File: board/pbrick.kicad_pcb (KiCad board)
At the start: 4 copper layers, 24 x 44 mm, 59 parts, among them J1 UJC-HP-3-SMT-TR, J2 TC2030-IDC-NL, J3 U.FL2PIN, J4 QWIIC, M0 5055680471, M1 5055680471, Q1 SSM6J507NU, Q2 SSM6J507NU, U1 MIC5219-3.3YML-TR, U2 ADP3330ARTZ-5-RL7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

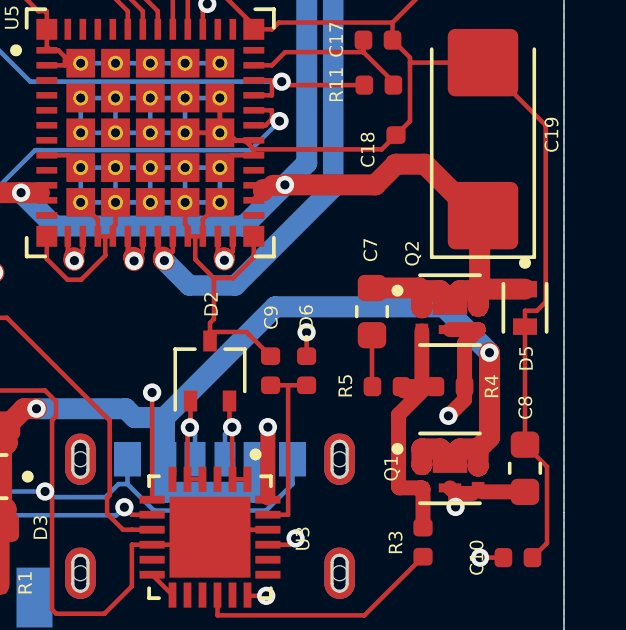
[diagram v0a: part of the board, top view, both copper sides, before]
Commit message: Correct schematic defect where Q2 was not routed on both ends
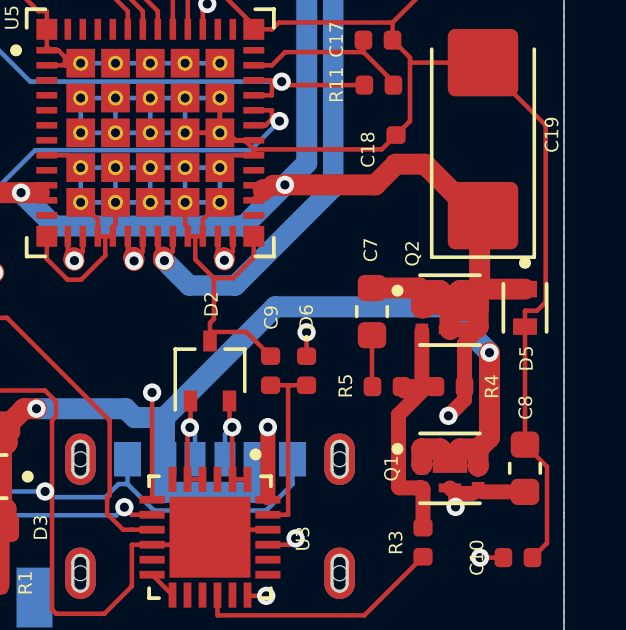
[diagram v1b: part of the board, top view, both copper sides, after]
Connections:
- C8 pad 2: Net-(C8-Pad2) -> VDD
- J1 pad S1: (no net) -> Net-(J1-PadS1)
- J1 pad S2: (no net) -> Net-(J1-PadS1)
- J1 pad S3: (no net) -> Net-(J1-PadS1)
- J1 pad S4: (no net) -> Net-(J1-PadS1)
- J2 pad 6: (no net) -> Net-(J2-Pad6)
- M0 pad S1: (no net) -> Net-(M0-PadS1)
- M0 pad S2: (no net) -> Net-(M0-PadS1)
- M1 pad S1: (no net) -> Net-(M1-PadS1)
- M1 pad S2: (no net) -> Net-(M1-PadS1)
- PROTEUS-III1 pad 13: (no net) -> /P1.08
- PROTEUS-III1 pad 14: (no net) -> /P1.09
- PROTEUS-III1 pad 15: (no net) -> /P0.11
- PROTEUS-III1 pad 16: (no net) -> /P0.12
- PROTEUS-III1 pad 17: (no net) -> /P0.03
- PROTEUS-III1 pad 7: (no net) -> /P0.02
- PROTEUS-III1 pad B4: (no net) -> /P1.00
- PROTEUS-III1 pad B5: (no net) -> /P0.21
- PROTEUS-III1 pad B6: (no net) -> /P0.07
- Q1 pad 4: Net-(C8-Pad2) -> VDD
- Q1 pad 8: Net-(C8-Pad2) -> VDD
- Q2 pad 4: Net-(C8-Pad2) -> VDD
- Q2 pad 8: Net-(C8-Pad2) -> VDD
- R4 pad 1: Net-(C8-Pad2) -> VDD
- U1 pad 5: (no net) -> Net-(U1-Pad5)
- U2 pad 3: (no net) -> Net-(U2-Pad3)
- U2 pad 5: (no net) -> Net-(U2-Pad5)
- U3 pad 11: (no net) -> Net-(U3-Pad11)
- U3 pad 14: (no net) -> Net-(U3-Pad14)
- U3 pad 15: (no net) -> Net-(U3-Pad15)
- U3 pad 17: (no net) -> Net-(U3-Pad17)
- U3 pad 19: (no net) -> Net-(U3-Pad19)
- U3 pad 20: (no net) -> Net-(U3-Pad20)
- U3 pad 24: Net-(C8-Pad2) -> VDD
- U3 pad 6: (no net) -> Net-(U3-Pad6)
- U5 pad 47: (no net) -> Net-(U5-Pad47)
- U5 pad 48: (no net) -> Net-(U5-Pad48)
- U6 pad 5: (no net) -> Net-(U6-Pad5)
- U7 pad 14: (no net) -> /PCA9624_7
- U7 pad 5: (no net) -> /PCA9624_0
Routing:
- net VDD: track 84.0 -> 106.9 mm, vias 3 -> 6
- net Net-(C8-Pad2): track 19.2 -> 0.00 mm, vias 3 -> 0

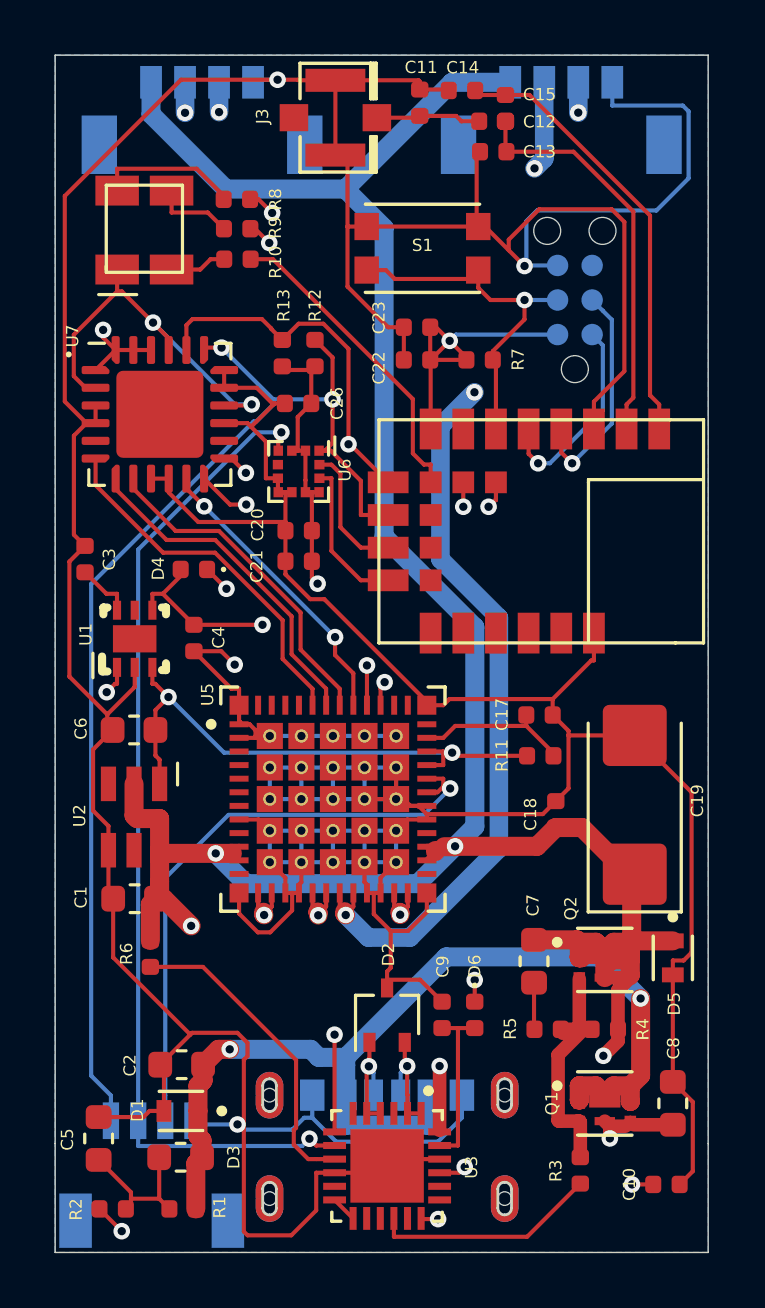
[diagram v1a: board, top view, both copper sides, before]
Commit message: 5v regulator has operational capacity from 2.7-20v (tested)   - removing extra diode and 2.7v line as 5v => 3.3v works at 5v input
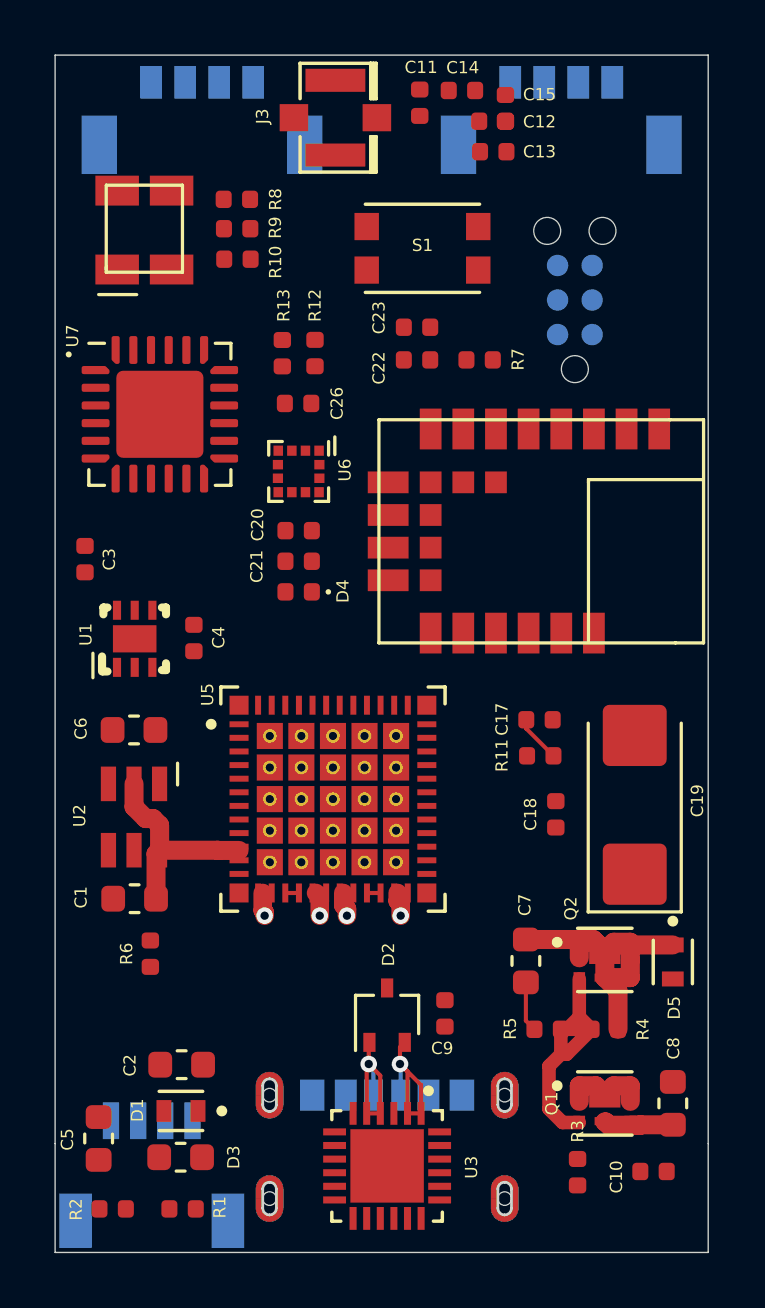
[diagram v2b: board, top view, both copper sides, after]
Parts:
- removed D6: D_Schottky, Diode_SMD:D_0402_1005Metric
- moved D4 3.94 mm to (128.9, 109.7)
- moved C10 0.67 mm to (142.0, 131.0)
- moved C7 0.30 mm to (137.3, 123.3)
- moved C17 0.17 mm to (137.8, 114.4)
- moved D5 0.15 mm to (142.7, 123.3)
- moved R3 0.12 mm to (139.2, 131.1)
- moved C9 0.12 mm to (134.3, 125.2)
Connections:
- net +2V8 renamed Net-(C9-Pad2)
- C22 pad 1: +3.3VA -> 3.3V
- C23 pad 1: +3.3VA -> 3.3V
- C4 pad 1: 3.3V -> Net-(C4-Pad1)
- D4 pad 1: +3.3VA -> 3.3V
- D4 pad 2: 3.3V -> Net-(C4-Pad1)
- J1 pad S1: Net-(J1-PadS1) -> (no net)
- J1 pad S2: Net-(J1-PadS1) -> (no net)
- J1 pad S3: Net-(J1-PadS1) -> (no net)
- J1 pad S4: Net-(J1-PadS1) -> (no net)
- J2 pad 1: +3.3VA -> 3.3V
- J2 pad 6: Net-(J2-Pad6) -> (no net)
- M0 pad S1: Net-(M0-PadS1) -> (no net)
- M0 pad S2: Net-(M0-PadS1) -> (no net)
- M1 pad S1: Net-(M1-PadS1) -> (no net)
- M1 pad S2: Net-(M1-PadS1) -> (no net)
- PROTEUS-III1 pad 13: /P1.08 -> (no net)
- PROTEUS-III1 pad 14: /P1.09 -> (no net)
- PROTEUS-III1 pad 15: /P0.11 -> (no net)
- PROTEUS-III1 pad 16: /P0.12 -> (no net)
- PROTEUS-III1 pad 17: /P0.03 -> (no net)
- PROTEUS-III1 pad 7: /P0.02 -> (no net)
- PROTEUS-III1 pad 8: +3.3VA -> 3.3V
- PROTEUS-III1 pad B4: /P1.00 -> (no net)
- PROTEUS-III1 pad B5: /P0.21 -> (no net)
- PROTEUS-III1 pad B6: /P0.07 -> (no net)
- R7 pad 1: +3.3VA -> 3.3V
- U1 pad 4: 3.3V -> Net-(C4-Pad1)
- U1 pad 5: Net-(U1-Pad5) -> (no net)
- U2 pad 3: Net-(U2-Pad3) -> (no net)
- U2 pad 5: Net-(U2-Pad5) -> (no net)
- U3 pad 11: Net-(U3-Pad11) -> (no net)
- U3 pad 14: Net-(U3-Pad14) -> (no net)
- U3 pad 15: Net-(U3-Pad15) -> (no net)
- U3 pad 17: Net-(U3-Pad17) -> (no net)
- U3 pad 19: Net-(U3-Pad19) -> (no net)
- U3 pad 20: Net-(U3-Pad20) -> (no net)
- U3 pad 6: Net-(U3-Pad6) -> (no net)
- U5 pad 47: Net-(U5-Pad47) -> (no net)
- U5 pad 48: Net-(U5-Pad48) -> (no net)
- U6 pad 5: Net-(U6-Pad5) -> (no net)
- U7 pad 14: /PCA9624_7 -> (no net)
- U7 pad 25: (no net) -> GND
- U7 pad 5: /PCA9624_0 -> (no net)
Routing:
- net GND: track 356.7 -> 1.00 mm, vias 5 -> 0
- net VDD: track 106.9 -> 24.4 mm, vias 6 -> 0
- net /P0.22: track 75.6 -> 0.00 mm, vias 3 -> 0
- net +3.3VA: track 56.9 -> 0.00 mm, vias 3 -> 0
- net /P0.19: track 53.5 -> 0.00 mm, vias 3 -> 0
- net 5V: track 52.9 -> 0.00 mm, vias 5 -> 0
- net 3.3V: track 50.9 -> 0.00 mm, vias 3 -> 0
- net /M1_0: track 41.5 -> 0.89 mm, vias 2 -> 1
- net /M0_0: track 40.7 -> 0.89 mm, vias 3 -> 1
- net VBUS: track 37.6 -> 3.29 mm, vias 2 -> 0
- net /M0_1: track 34.9 -> 0.88 mm, vias 2 -> 1
- net /M1_1: track 33.7 -> 0.86 mm, vias 2 -> 1
- net /ANT: track 16.3 -> 0.00 mm
- net /P0.09: track 16.1 -> 0.00 mm, vias 2 -> 0
- net /RF: track 14.8 -> 0.00 mm
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- removed copper zone on B.Cu, net GND
- removed copper zone on GND, net GND
- removed copper zone on M.Cu, net GND
- removed copper zone on M.Cu, net VBUS
- removed copper zone on M.Cu, net VDD

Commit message: Updating PCB routing
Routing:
- net GND: track 1.00 -> 303.0 mm, vias 0 -> 3
- net VDD: track 24.4 -> 112.5 mm, vias 0 -> 4
- net 3.3V: track 0.00 -> 63.0 mm, vias 0 -> 3
- net /P0.19: track 0.00 -> 55.3 mm, vias 0 -> 3
- net /P0.22: track 0.00 -> 51.8 mm, vias 0 -> 3
- net 5V: track 0.00 -> 49.8 mm, vias 0 -> 5
- net /M1_0: track 0.89 -> 36.3 mm, vias 1 -> 2
- net /M0_0: track 0.89 -> 36.1 mm, vias 1 -> 2
- net /M1_1: track 0.86 -> 35.4 mm, vias 1 -> 2
- net /M0_1: track 0.88 -> 34.2 mm
- net VBUS: track 3.29 -> 32.9 mm, vias 0 -> 2
- net /P0.09: track 0.00 -> 16.3 mm, vias 0 -> 2
- net /ANT: track 0.00 -> 15.9 mm
- net /RF: track 0.00 -> 14.4 mm
- net Net-(R2-Pad2): track 0.00 -> 13.8 mm, vias 0 -> 2
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- added copper zone on B.Cu, net GND
- added copper zone on GND, net GND
- added copper zone on M.Cu, net GND
- added copper zone on M.Cu, net VBUS
- added copper zone on M.Cu, net VDD

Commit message: Updating PCB layout
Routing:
- net VDD: track 112.5 -> 106.7 mm, vias 4 -> 5
- net VBUS: track 32.9 -> 37.4 mm
- net GND: track 303.0 -> 307.0 mm

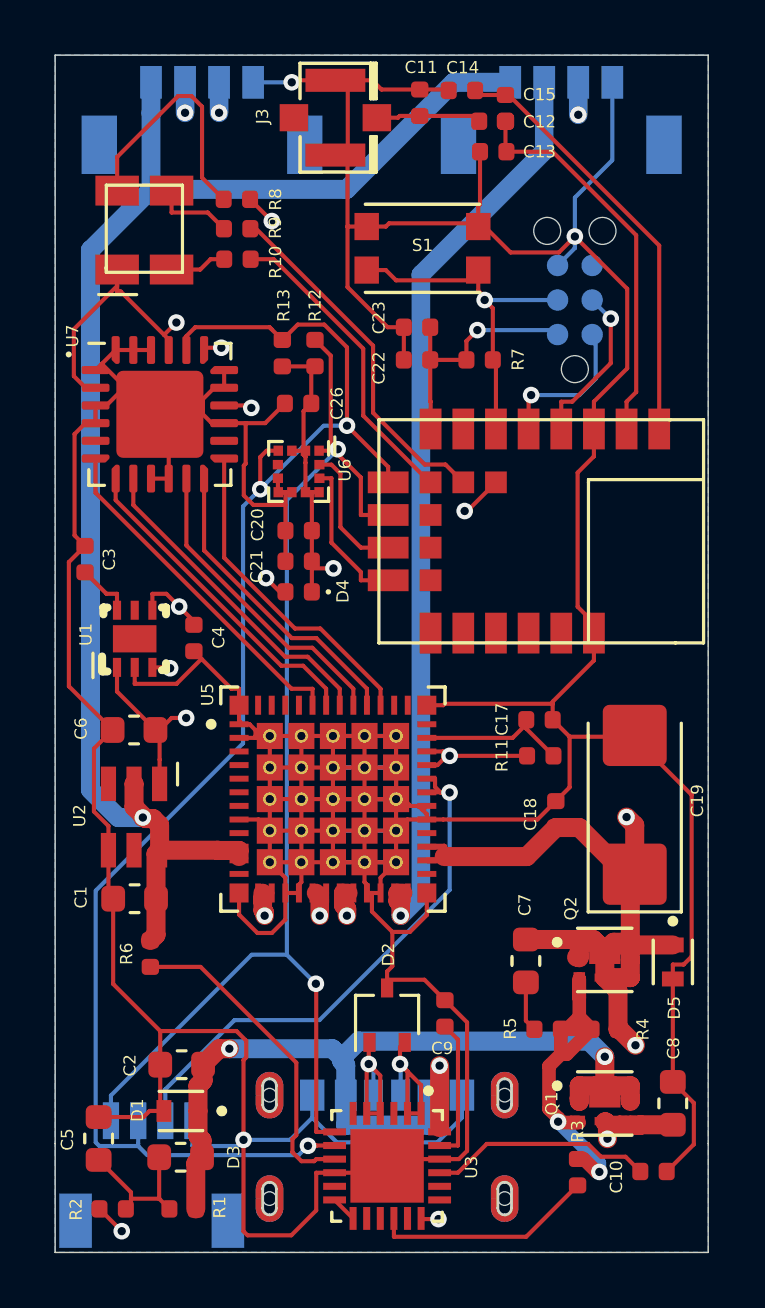
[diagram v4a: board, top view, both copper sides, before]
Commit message: Updating PCB to resolve an issue with PCA9624 OE being HIGH instead of Controller - Added PCA9624 library definition (untested) - Convert pbrick_motor to use PCA9624 driver
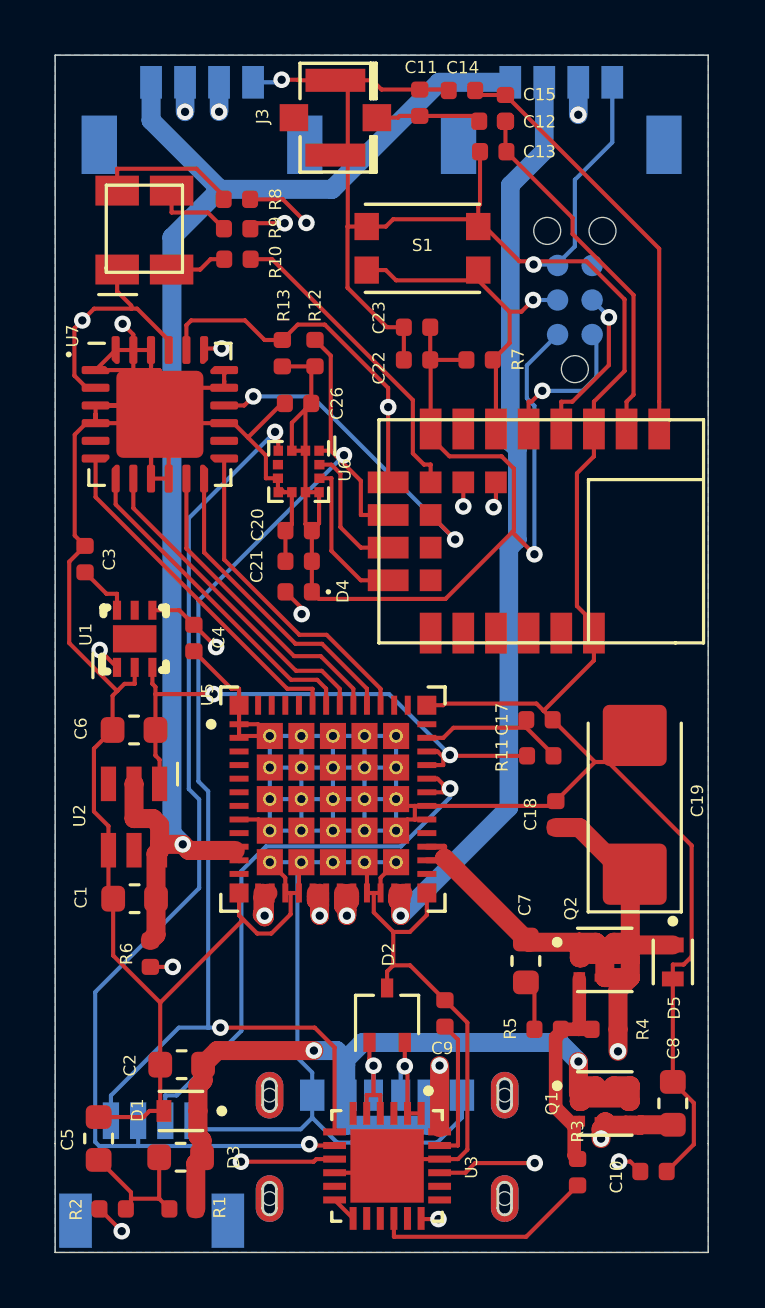
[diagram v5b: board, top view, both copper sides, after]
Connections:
- J2 pad 6: (no net) -> Net-(J2-Pad6)
- PROTEUS-III1 pad 13: (no net) -> /P1.08
- PROTEUS-III1 pad 14: (no net) -> /P1.09
- PROTEUS-III1 pad 15: (no net) -> /P0.11
- PROTEUS-III1 pad 16: (no net) -> /P0.12
- PROTEUS-III1 pad 17: (no net) -> /P0.03
- PROTEUS-III1 pad 7: (no net) -> /P0.02
- PROTEUS-III1 pad B4: (no net) -> /P1.00
- PROTEUS-III1 pad B5: (no net) -> /P0.21
- PROTEUS-III1 pad B6: (no net) -> /P0.07
- U1 pad 5: (no net) -> Net-(U1-Pad5)
- U2 pad 3: (no net) -> Net-(U2-Pad3)
- U2 pad 5: (no net) -> Net-(U2-Pad5)
- U3 pad 11: (no net) -> Net-(U3-Pad11)
- U3 pad 14: (no net) -> Net-(U3-Pad14)
- U3 pad 15: (no net) -> Net-(U3-Pad15)
- U3 pad 17: (no net) -> Net-(U3-Pad17)
- U3 pad 19: (no net) -> Net-(U3-Pad19)
- U3 pad 20: (no net) -> Net-(U3-Pad20)
- U3 pad 6: (no net) -> Net-(U3-Pad6)
- U5 pad 47: (no net) -> Net-(U5-Pad47)
- U5 pad 48: (no net) -> Net-(U5-Pad48)
- U6 pad 5: (no net) -> Net-(U6-Pad5)
- U7 pad 14: (no net) -> /PCA9624_7
- U7 pad 16: 5V -> /P1.00
- U7 pad 5: (no net) -> /PCA9624_0
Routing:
- net GND: track 307.0 -> 325.3 mm
- net 3.3V: track 63.0 -> 75.3 mm, vias 3 -> 2
- net /P1.00: track 0.00 -> 12.1 mm, vias 0 -> 2
- net Net-(Q1-Pad3): track 14.7 -> 8.53 mm, vias 2 -> 0
- net /M0_0: track 36.1 -> 40.3 mm
- net Net-(LED1-Pad3): track 9.18 -> 5.26 mm
- net VBUS: track 37.4 -> 33.5 mm
- net /P0.19: track 55.8 -> 59.7 mm
- net /M1_0: track 36.3 -> 38.7 mm
- net Net-(D2-Pad2): track 6.59 -> 4.28 mm
- net VDD: track 106.7 -> 108.9 mm, vias 5 -> 4
- net /P0.10: track 13.1 -> 15.4 mm, vias 0 -> 2
- net 5V: track 49.8 -> 47.9 mm, vias 5 -> 4
- net Net-(D2-Pad1): track 6.36 -> 4.93 mm
- net /M1_1: track 35.4 -> 34.1 mm
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- removed copper zone on M.Cu, net GND

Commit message: Updating layout
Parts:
- added 3V3: Val**, Connectors:PAD.02X.02, F.Cu at (129.4, 110.8)
- added 5V: Val**, Connectors:PAD.02X.02, F.Cu at (122.3, 99.4)
- added VBUS: Val**, Connectors:PAD.02X.02, F.Cu at (138.0, 128.1)
- added VDD: Val**, Connectors:PAD.02X.02, F.Cu at (138.4, 119.5)
- U7: footprint Package_DFN_QFN:QFN-24-1EP_5x5mm_P0.65mm_EP3.2x3.2mm -> Package_DFN_QFN:QFN-24-1EP_4x4mm_P0.5mm_EP2.65x2.65mm_ThermalVias
- moved C13 1.46 mm to (134.9, 94.5)
- moved C12 1.46 mm to (134.9, 93.3)
- moved C15 1.46 mm to (135.4, 92.8)
- moved R8 1.10 mm to (126.7, 96.4)
- moved R9 1.08 mm to (126.7, 95.3)
- moved C23 0.93 mm to (133.8, 100.8)
- moved R7 0.87 mm to (136.1, 102.0)
- moved C22 0.87 mm to (133.8, 102.0)
- moved J2 0.45 mm to (138.7, 99.2)
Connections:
- J2 pad 6: Net-(J2-Pad6) -> (no net)
- U3 pad 12: Earth -> GND
- U3 pad 13: Earth -> GND
- U3 pad 22: GND -> 3.3V
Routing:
- net GND: track 325.3 -> 239.1 mm, vias 3 -> 8
- net VDD: track 108.9 -> 76.0 mm, vias 4 -> 7
- net 3.3V: track 75.3 -> 91.1 mm, vias 2 -> 5
- net /P0.19: track 59.7 -> 52.7 mm
- net Net-(C9-Pad2): track 5.24 -> 11.7 mm
- net /P0.22: track 52.6 -> 59.0 mm
- net 5V: track 47.9 -> 42.8 mm, vias 4 -> 3
- net /VBUS_EN_SNK: track 8.21 -> 12.6 mm, vias 0 -> 2
- net /SWDCLK: track 5.96 -> 10.3 mm
- net Net-(Q1-Pad3): track 8.53 -> 12.8 mm, vias 0 -> 2
- net /M0_0: track 40.3 -> 44.0 mm
- net /M1_1: track 34.1 -> 37.7 mm
- net VBUS: track 33.5 -> 30.3 mm, vias 2 -> 3
- net /SWDIO: track 5.50 -> 8.62 mm
- net Net-(C10-Pad2): track 7.70 -> 10.5 mm, vias 2 -> 0
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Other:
- board text added: "PBRICK - PROTEUS III - REVISION X"
- board text removed: "PBRICK - PROTEUS III - REVISION IX"

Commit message: Updating board, definitions
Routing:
- net /P0.22: track 59.0 -> 53.3 mm
- net VBUS: track 30.3 -> 34.7 mm
- net 5V: track 42.8 -> 46.1 mm
- net GND: track 239.1 -> 236.4 mm
- net Net-(D2-Pad2): track 4.30 -> 6.30 mm
- net Net-(D2-Pad1): track 4.34 -> 6.30 mm
- net /P0.19: track 52.7 -> 54.2 mm
